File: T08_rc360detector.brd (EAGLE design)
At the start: 100 x 80 mm, 45 parts, among them IC1 LM317MSTT3, IC2 LM317MSTT3, U2 ATMEGA328P_PDIP, X1 SSW-101-02-S-D, X2 332-04, X3 SSW-101-02-S-D, X4 87758-0616, X5 87758-0616

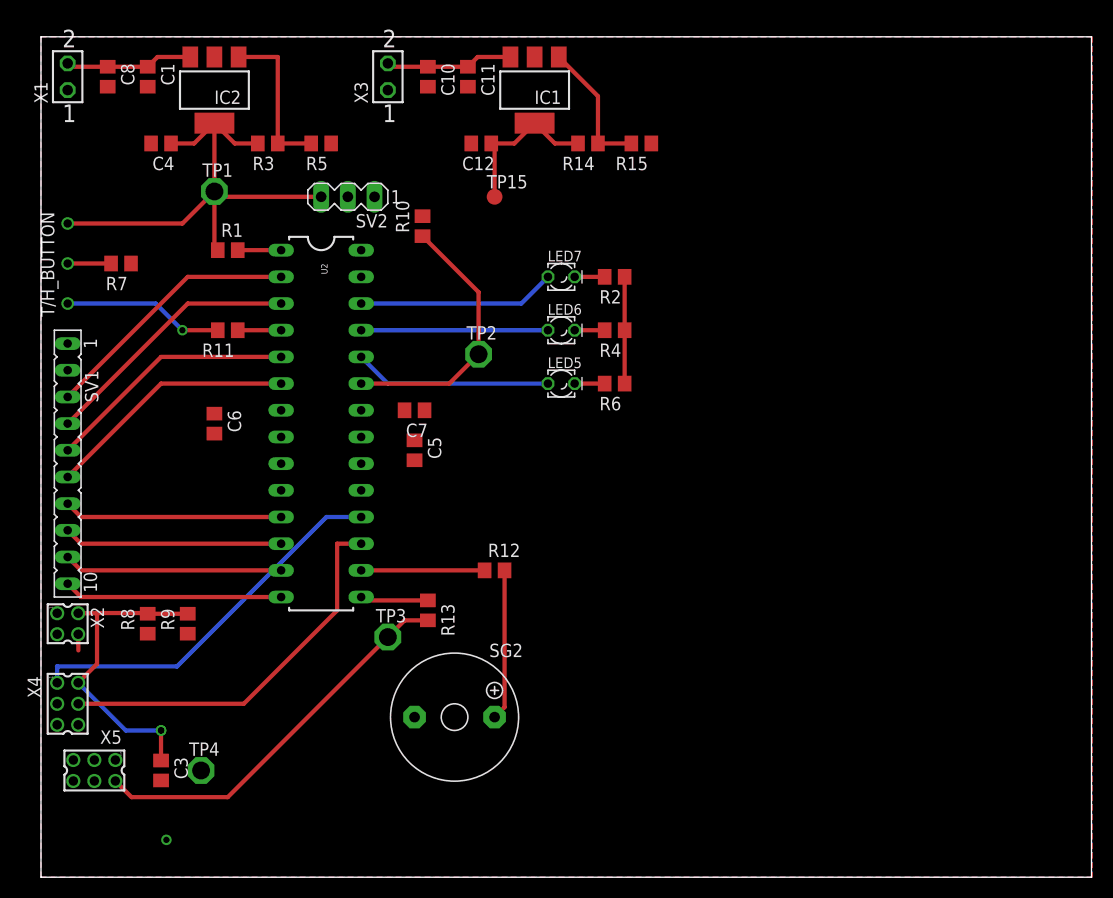
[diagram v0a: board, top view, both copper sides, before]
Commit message: 2nd pass
-Added custom library that contains button and buzzer
-Routed rest of connections. Left TWI interface out until Jared adds the
finished connections to the schematic
-Added screw holes, can resize if we want bigger screws
-Added some basic silk screen
-Added jumper for servo so we can switch it between if needed.
-Still need to find actual LEDs, until then there are generic T/H
-Havnt touched DRC, must look into in future
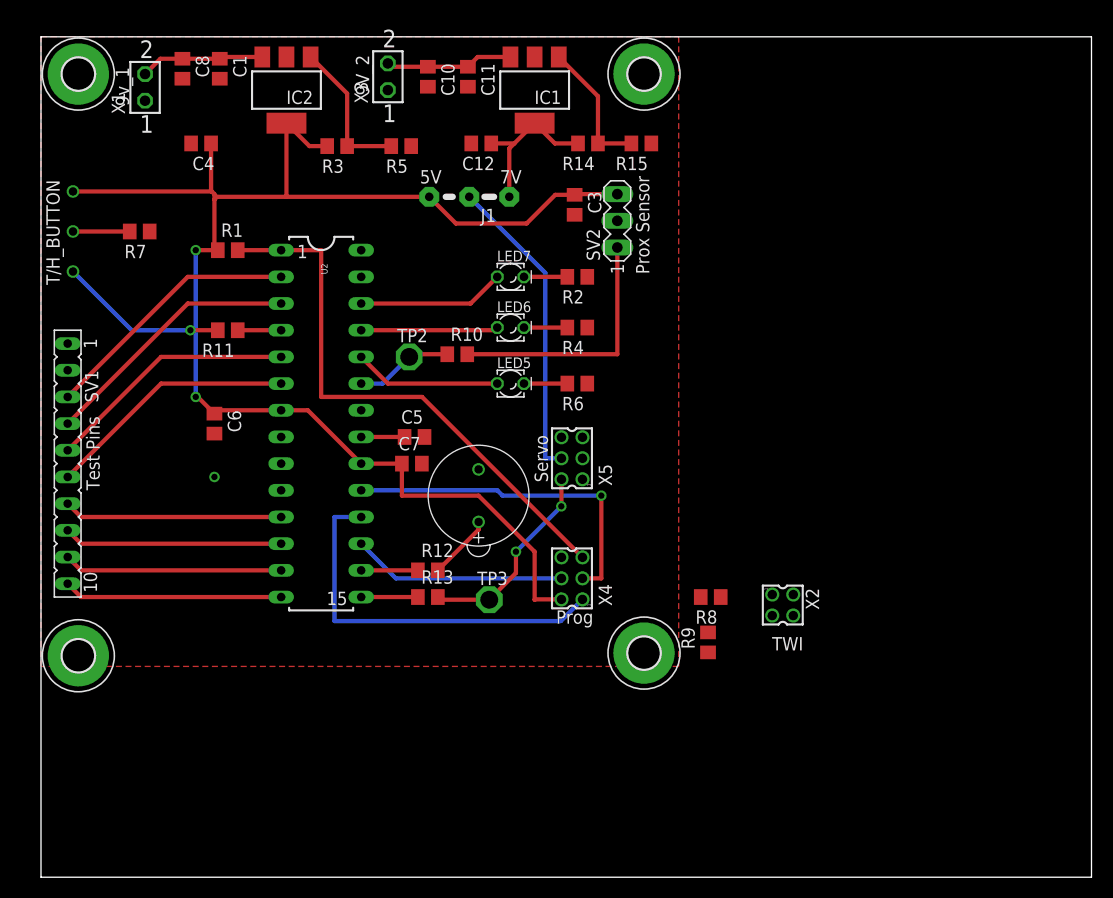
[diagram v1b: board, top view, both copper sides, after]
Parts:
- removed SG2: F/TMB, buzzer:F/TMB
- removed TP1, TP4: TPPAD1-17, testpad:P1-17
- removed TP15: TPTP15R, testpad:TP15R
- added CX-0905C: CX-0905C, 360prox:BUZZER_CX-0905C
- added H1, H2, H3, H4: MOUNT-PAD-ROUND3.0, holes:3,0-PAD
- added J1: (no value), jumper:04C
- moved X2 68.1 mm to (70.6, 25.9)
- moved C3 66.7 mm to (50.8, 64.0)
- moved X5 54.3 mm to (50.5, 39.9), turned to 90 degrees
- moved R8 53.7 mm to (63.8, 26.7), turned to 180 degrees
- moved R9 49.6 mm to (63.5, 22.4)
- moved X4 49.5 mm to (50.5, 28.4), turned to 90 degrees
- moved SV2 25.8 mm to (54.9, 62.5), turned to 90 degrees
- moved R10 12.6 mm to (39.6, 49.8), turned to 0 degrees
- moved TP3 10.3 mm to (42.7, 26.4)
- moved R5 7.62 mm to (34.3, 69.6)
- moved X1 7.44 mm to (9.91, 75.2)
- moved C8 7.15 mm to (13.5, 77.0)
- moved C1 6.90 mm to (17.0, 77.0)
- moved IC2 6.86 mm to (23.4, 74.9)
- moved R3 6.61 mm to (28.2, 69.6)
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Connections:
- new net N$16: J1.2, X5.4
- net +5V: now also J1.3; no longer TP1.TP
- net GND: now also CX-0905C.P$2, H1.B3,0, H2.B3,0, H3.B3,0, H4.B3,0; no longer SG2.-, TP4.TP
- net N$4: now also CX-0905C.P$1; no longer SG2.+
- net VCC: now also J1.1; no longer TP15.TP, X5.4
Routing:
- net +5V: track 78.2 -> 139.7 mm, vias 1 -> 2
- net PROG_TRST: track 4.13 -> 53.1 mm
- net PROG_SCK: track 0.00 -> 32.7 mm, vias 0 -> 1
- net N$16: track 0.00 -> 29.4 mm
- net PROX_ANALOG: track 0.00 -> 24.5 mm
- net SERVO_PWM: track 37.4 -> 19.3 mm, vias 0 -> 2
- net PROG_MOSI: track 37.0 -> 20.4 mm
- net N$9: track 25.8 -> 9.35 mm
- net GND: track 12.6 -> 0.00 mm
- net N$4: track 14.4 -> 6.22 mm
- net N$10: track 11.7 -> 5.40 mm
- net LED2: track 18.8 -> 14.0 mm
- net LED0: track 18.8 -> 14.0 mm
- net LED1: track 17.8 -> 13.1 mm
- net AREF: track 0.00 -> 4.13 mm
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- removed copper zone on layer 16, net GND
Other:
- board text added: "1"
- board text added: "15"
- board text added: "5V"
- board text added: "7V"
- board text added: "9V_2"
- board text added: "9v_1"
- board text added: "Prog"
- board text added: "Prox Sensor"
- board text added: "Servo"
- board text added: "TWI"
- board text added: "Test Pins"

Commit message: Update
Rerouted layout with new TWI circuitry. The logic converter IC is so
small the chip doesnt pass DRC, so I informed Jared and he's looking
into an alternate solution. Also the current chip is PDIP but I'm
debating changing it to TQFP. Will need to discuss tomorrow.
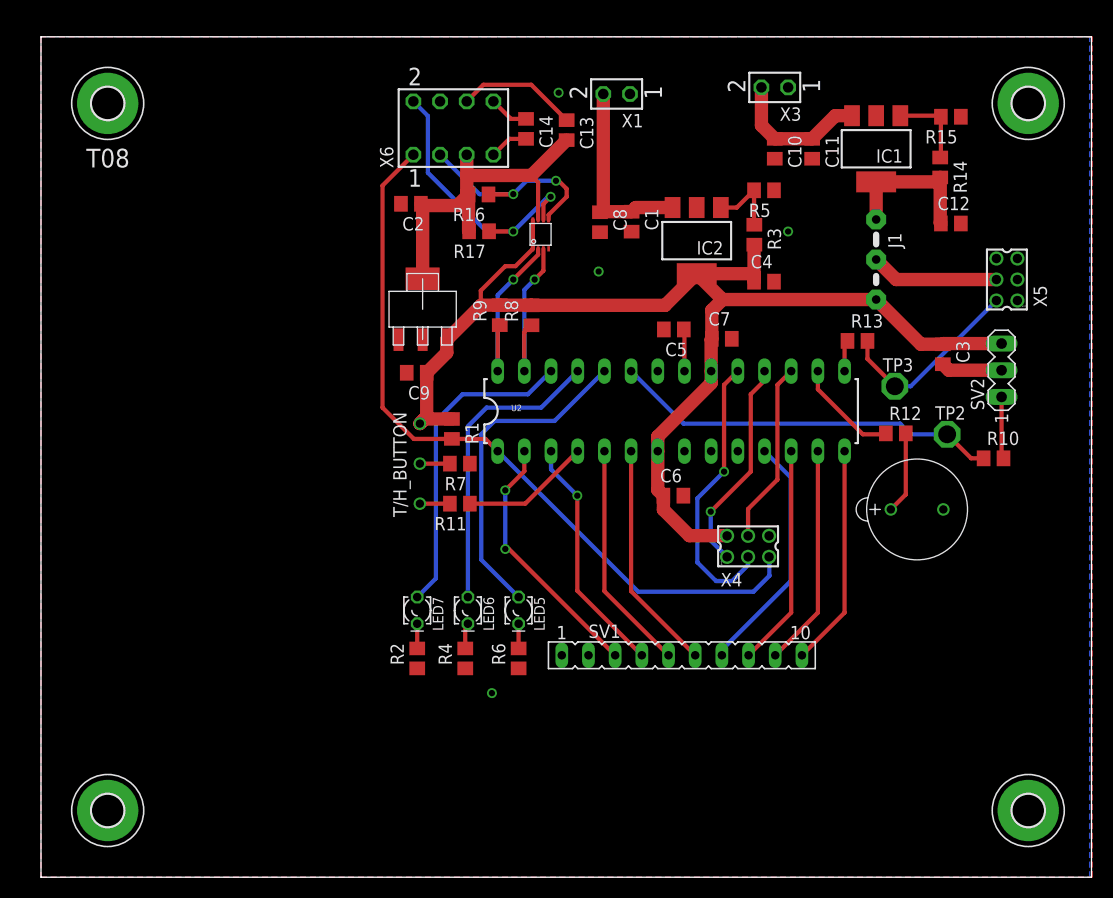
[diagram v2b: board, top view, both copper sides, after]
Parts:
- removed X2: 332-04, con-garry:332-04
- added C13, C14, C9: .1u, resistor:C0805
- added C2: 10u, rcl:C0805
- added R16, R17: 4.7k, rcl:R0805
- added U$1: LM1117, 360prox:SOT-223
- added U3: PCA9306, SparkFun-DigitalIC:PSOP-8
- added X6: SSW-104-02-S-Q, con-samtec:SSW-104-02-S-Q
- C3: value 10uF -> 10u
- R15: value 912 -> 1.1k
- R2, R4, R6: value 220 -> 240
- moved SV1 61.2 mm to (61.0, 21.1), turned to 0 degrees
- moved C4 55.2 mm to (68.8, 56.7), turned to 0 degrees
- moved R10 52.0 mm to (90.7, 39.9)
- moved TP2 51.7 mm to (86.3, 42.2)
- moved R13 47.6 mm to (77.7, 51.1)
- moved R12 46.4 mm to (81.4, 42.3)
- moved C12 45.3 mm to (86.6, 62.2), turned to 0 degrees
- moved X1 44.9 mm to (54.8, 74.6), turned to 90 degrees
- moved X5 44.8 mm to (91.9, 56.9)
- moved C6 44.2 mm to (60.2, 36.3), turned to 0 degrees
- moved TP3 43.6 mm to (81.3, 46.7)
- moved C8 42.4 mm to (53.2, 62.4)
- moved C1 41.8 mm to (56.2, 62.4)
- moved CX-0905C 41.8 mm to (83.4, 35.0), turned to 90 degrees
- moved IC2 41.6 mm to (62.4, 60.6)
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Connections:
- net N$10 renamed BUZZER
- net N$11 renamed SERVO_PWM_R
- net N$3 renamed BUTTON_5V_R
- net N$5 renamed LED0_R
- net N$6 renamed BUTTON_5V
- net N$7 renamed LED1_R
- net N$8 renamed LED2_R
- net N$9 renamed PROX_ANALOG_R
- new net +3V3: C13.2, C2.1, R16.2, R17.2, U$1.VOUT, U3.7, X6.5
- new net N$18: C13.1, X6.6
- new net N$19: C14.2, X6.7
- new net N$20: C14.1, X6.8
- new net SCL_BUF: R17.1, U3.6, X6.2
- new net SDA_BUF: R16.1, U3.5, X6.3
- net +5V: now also C9.1, U$1.INPUT, U3.1, U3.8; no longer X2.2
- net GND: now also C2.2, C9.2, U$1.GND/ADJ, U3.4, X6.4; no longer X2.4
- net PROG_TRST: now also X6.1
- net TWI_SCL: now also U3.2; no longer X2.3
- net TWI_SDA: now also U3.3; no longer X2.1
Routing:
- net +3V3: track 0.00 -> 34.8 mm
- net PROX_ANALOG_R: track 9.35 -> 37.0 mm
- net SCL_BUF: track 0.00 -> 27.5 mm, vias 0 -> 2
- net SDA_BUF: track 0.00 -> 20.5 mm, vias 0 -> 2
- net +5V: track 139.7 -> 120.9 mm, vias 2 -> 0
- net PROG_TRST: track 53.1 -> 71.8 mm
- net PROX_ANALOG: track 24.5 -> 5.92 mm
- net TWI_SCL: track 0.00 -> 17.7 mm, vias 0 -> 1
- net N$16: track 29.4 -> 12.2 mm
- net LED0: track 14.0 -> 31.2 mm
- net TWI_SDA: track 0.00 -> 17.0 mm, vias 0 -> 1
- net PROG_MISO: track 36.9 -> 20.4 mm, vias 0 -> 1
- net LED2: track 14.0 -> 30.4 mm
- net LED1: track 13.1 -> 28.9 mm
- net BUTTON_5V: track 16.1 -> 2.86 mm, vias 1 -> 0
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- added copper zone on layer 16, net GND
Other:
- board text added: "T08"
- board text removed: "1"
- board text removed: "15"
- board text removed: "5V"
- board text removed: "7V"
- board text removed: "9V_2"
- board text removed: "9v_1"
- board text removed: "Prog"
- board text removed: "Prox Sensor"
- board text removed: "Servo"
- board text removed: "TWI"
- board text removed: "Test Pins"
